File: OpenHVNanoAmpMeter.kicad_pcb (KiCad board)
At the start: 4 copper layers, 64.5 x 38 mm, 70 parts, among them J1 Conn_Coaxial, J2 Conn_Coaxial, J3 AVR-ISP-6, J4 Barrel_Jack_Switch, U1 DDC112U, U10 NCP1117-5.0_SOT223, U11 NCP1117-5.0_SOT223, U2 ATmega328PB-M, U3 74LV8154, U4 74LS151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

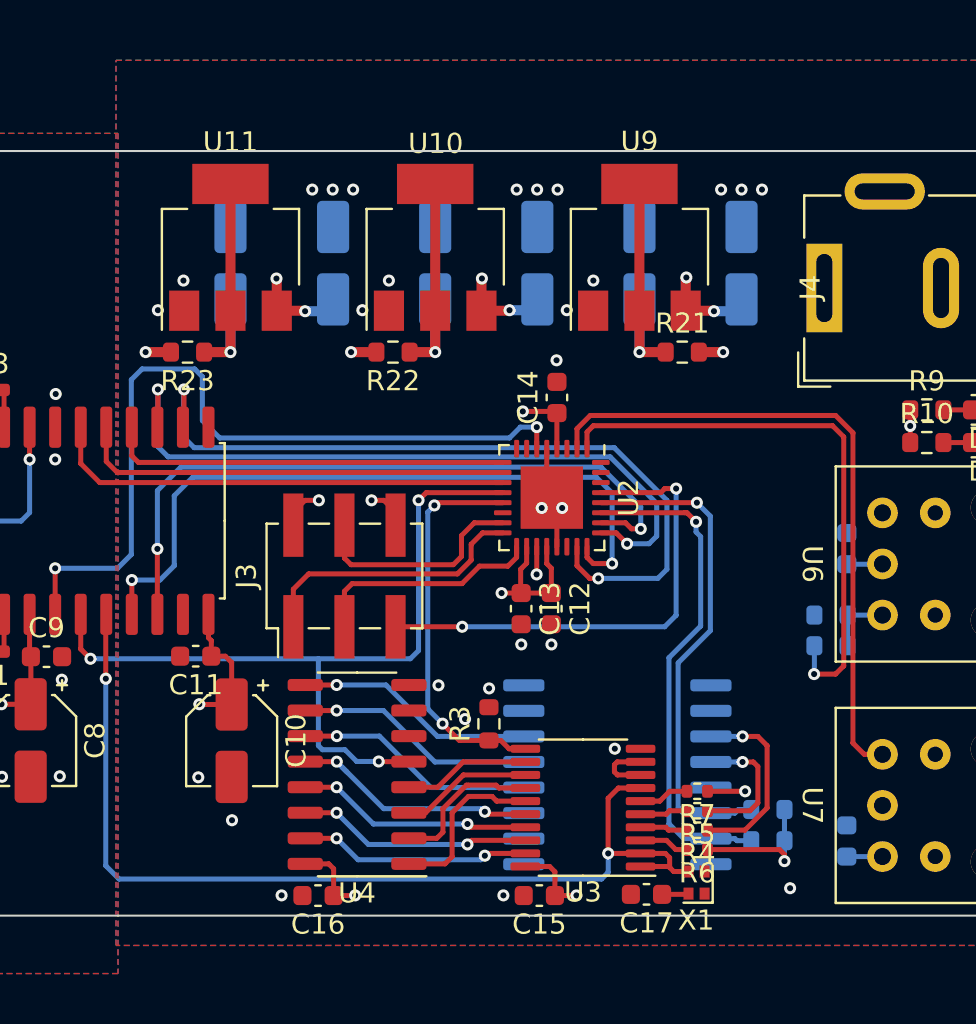
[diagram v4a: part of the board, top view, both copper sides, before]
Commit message: updated 10MHz oscillator to DIP 14 package
needs larger PCB space, but much easier to purchase
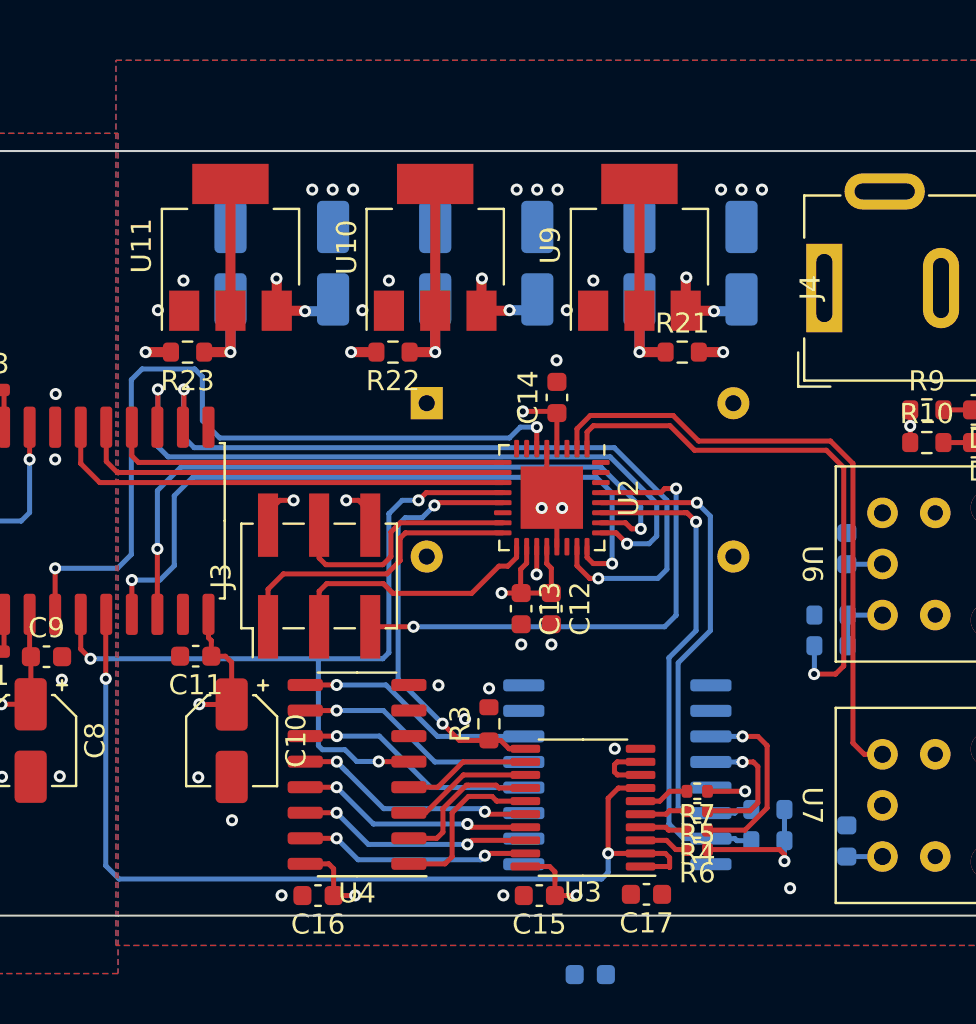
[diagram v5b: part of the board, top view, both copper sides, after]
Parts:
- added C28: 100n, Capacitor_SMD:C_0603_1608Metric, B.Cu at (96.4, 74.9)
- X1: value ASCO -> CXO_DIP14; footprint Oscillator:Oscillator_SMD_Abracon_ASCO-4Pin_1.6x1.2mm -> Oscillator:Oscillator_DIP-14; moved to B.Cu
- moved X1 27.3 mm to (88.3, 46.5), turned to 0 degrees
- moved J3 1.26 mm to (82.9, 55.1)
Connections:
- X1 pad 1: unconnected-(X1-Pad1) -> +5VD
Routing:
- net +3V3: track 16.7 -> 4.74 mm
- net /Clock Generation/CNT_CLR: track 19.4 -> 21.1 mm
- net /DataProcessing/SCK: track 11.5 -> 13.2 mm
- net /DataProcessing/MISO: track 13.9 -> 15.3 mm
- net /DataProcessing/MOSI: track 11.1 -> 12.5 mm
- net +5VD: track 38.8 -> 37.5 mm
- net /DataProcessing/~{RESET}: track 24.3 -> 25.6 mm
- net /Clock Generation/CLK_10MHz: track 49.5 -> 48.4 mm
- net /DataProcessing/LWLRX: track 32.5 -> 31.6 mm
- net /DataProcessing/LWLTX: track 28.4 -> 27.5 mm

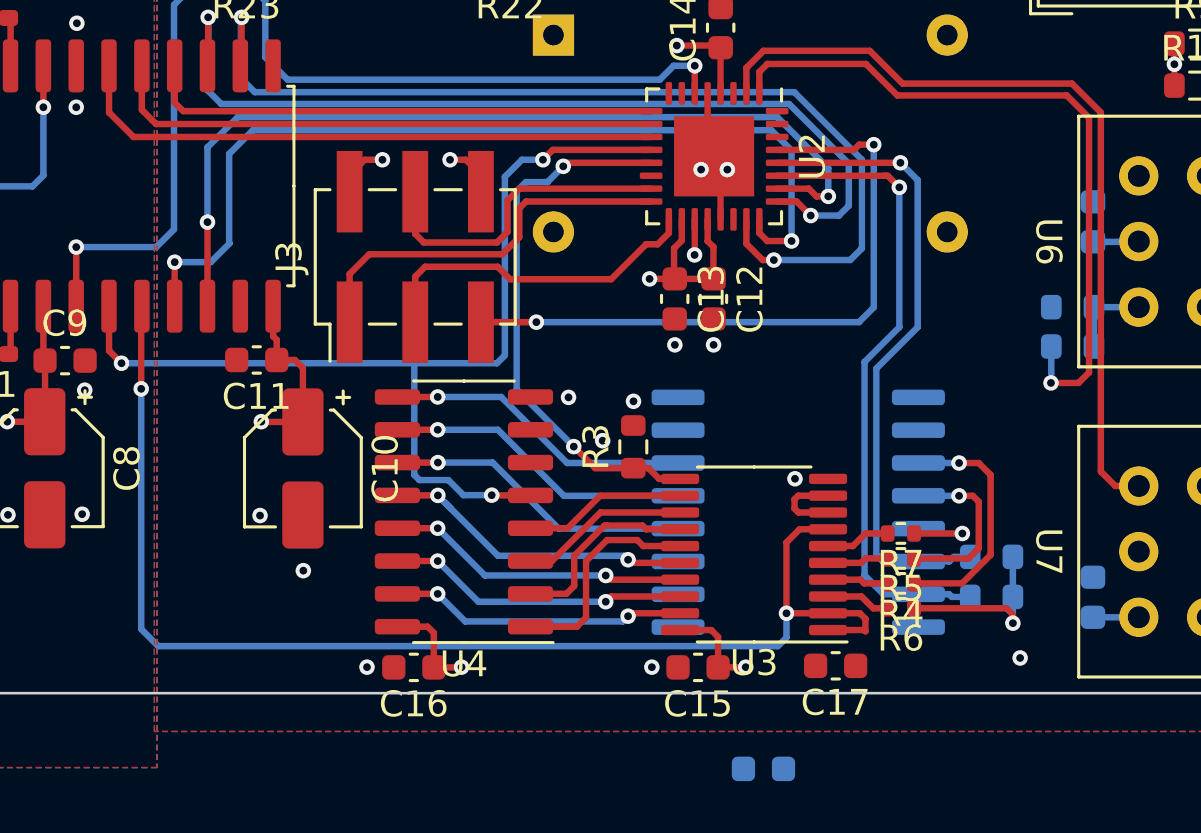
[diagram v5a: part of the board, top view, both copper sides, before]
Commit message: inlcuded buffer for 10MHz clock
otherwise the oscillator does not have enough drive strength
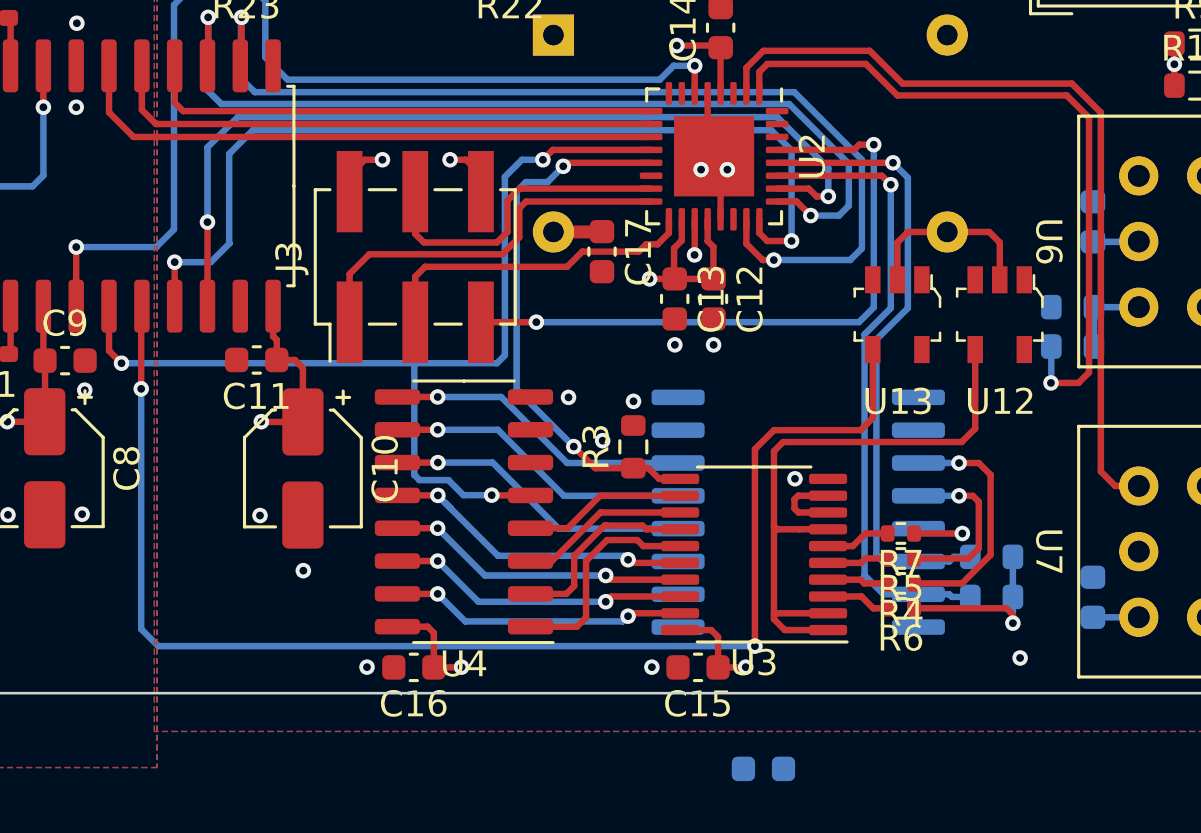
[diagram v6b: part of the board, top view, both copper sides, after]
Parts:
- added U12: SN74LVC1G17DBVR, digikey-footprints:SOT-753, F.Cu at (105.6, 57.4)
- added U13: SN74LVC1G17DBVR, digikey-footprints:SOT-753, F.Cu at (101.6, 57.4)
- moved C17 18.4 mm to (90.2, 54.9), turned to -90 degrees
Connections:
- U3 pad 1: /Clock Generation/CLK_10MHz -> Net-(U3-Pad1)
- U3 pad 2: /Clock Generation/CLK_10MHz -> Net-(U3-Pad1)
- U3 pad 7: /Clock Generation/CLK_10MHz -> Net-(U3-Pad1)
- X1 pad 8: /Clock Generation/CLK_10MHz -> Net-(X1-Pad8)
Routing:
- net Net-(U3-Pad1): track 0.00 -> 24.2 mm
- net Net-(X1-Pad8): track 0.00 -> 7.19 mm
- net /Clock Generation/CLK_10MHz: track 48.4 -> 51.8 mm
- net +5VD: track 37.5 -> 39.4 mm

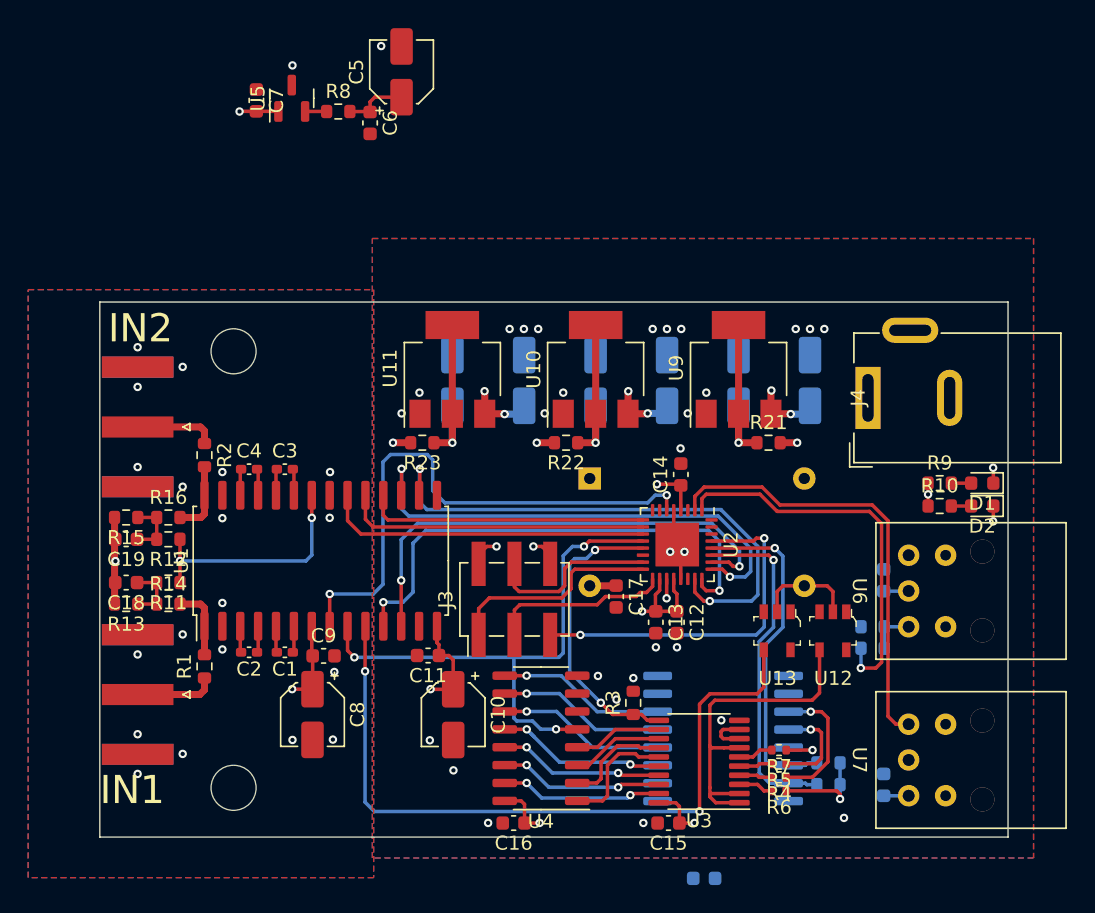
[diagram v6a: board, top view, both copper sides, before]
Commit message: added buffer to ref voltage generation
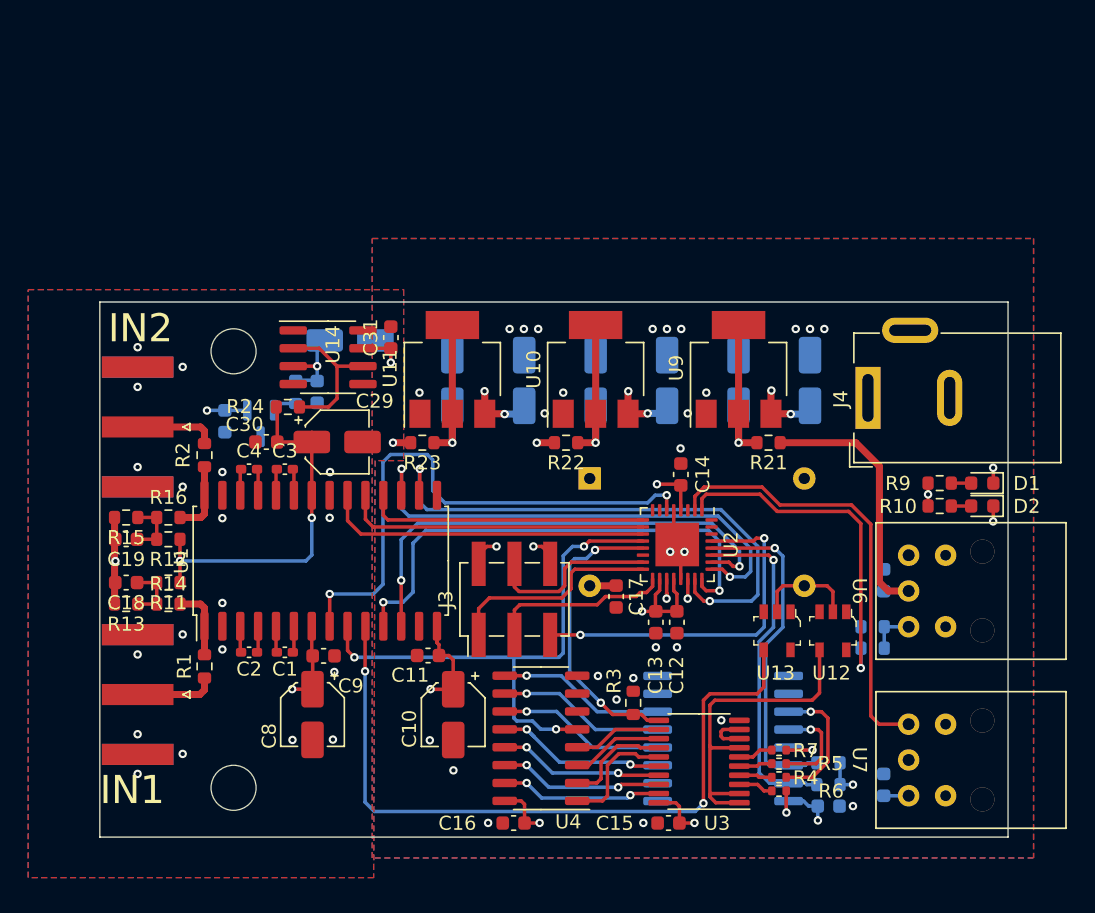
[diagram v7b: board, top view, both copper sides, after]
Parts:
- added C29: 10u, Capacitor_SMD:CP_Elec_4x3.9, F.Cu at (70.4, 43.9)
- added C30: 100n, Capacitor_SMD:C_0603_1608Metric, F.Cu at (65.3, 43.9)
- added C31: 100n, Capacitor_SMD:C_0603_1608Metric, F.Cu at (74.2, 36.5)
- added R24: R, Resistor_SMD:R_0603_1608Metric, F.Cu at (66.9, 41.5)
- added U14: OPA340UA, Package_SO:SOIC-8_3.9x4.9mm_P1.27mm, F.Cu at (69.7, 37.9)
- C5, C6, C7, R8, U5: moved to B.Cu
- moved U5 23.2 mm to (64.9, 42.6), turned to -90 degrees
- moved C7 22.9 mm to (62.4, 42.5), turned to 90 degrees
- moved R8 20.1 mm to (67.4, 40.4), turned to 90 degrees
- moved C6 19.5 mm to (68.9, 40.4)
- moved C5 19.4 mm to (71.3, 36.7), turned to 0 degrees
- moved C28 10.2 mm to (105.3, 69.8), turned to 0 degrees
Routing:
- net Net-(D1-Pad1): track 1.10 -> 32.7 mm, vias 1 -> 2
- net Net-(D2-Pad1): track 2.48 -> 32.2 mm
- net +3V3: track 4.74 -> 21.8 mm, vias 1 -> 0
- net Net-(R24-Pad1): track 0.00 -> 10.7 mm
- net /CurrentMeasurement/VREF: track 16.9 -> 26.2 mm
- net +5VA: track 10.6 -> 13.7 mm, vias 3 -> 4
- net /DataProcessing/LWLTX: track 27.5 -> 24.8 mm
- net Net-(C5-Pad1): track 4.49 -> 5.72 mm, vias 0 -> 1
- net +5VD: track 39.4 -> 39.8 mm, vias 10 -> 12
- net GNDA: vias 22 -> 20
- net GND: vias 30 -> 29

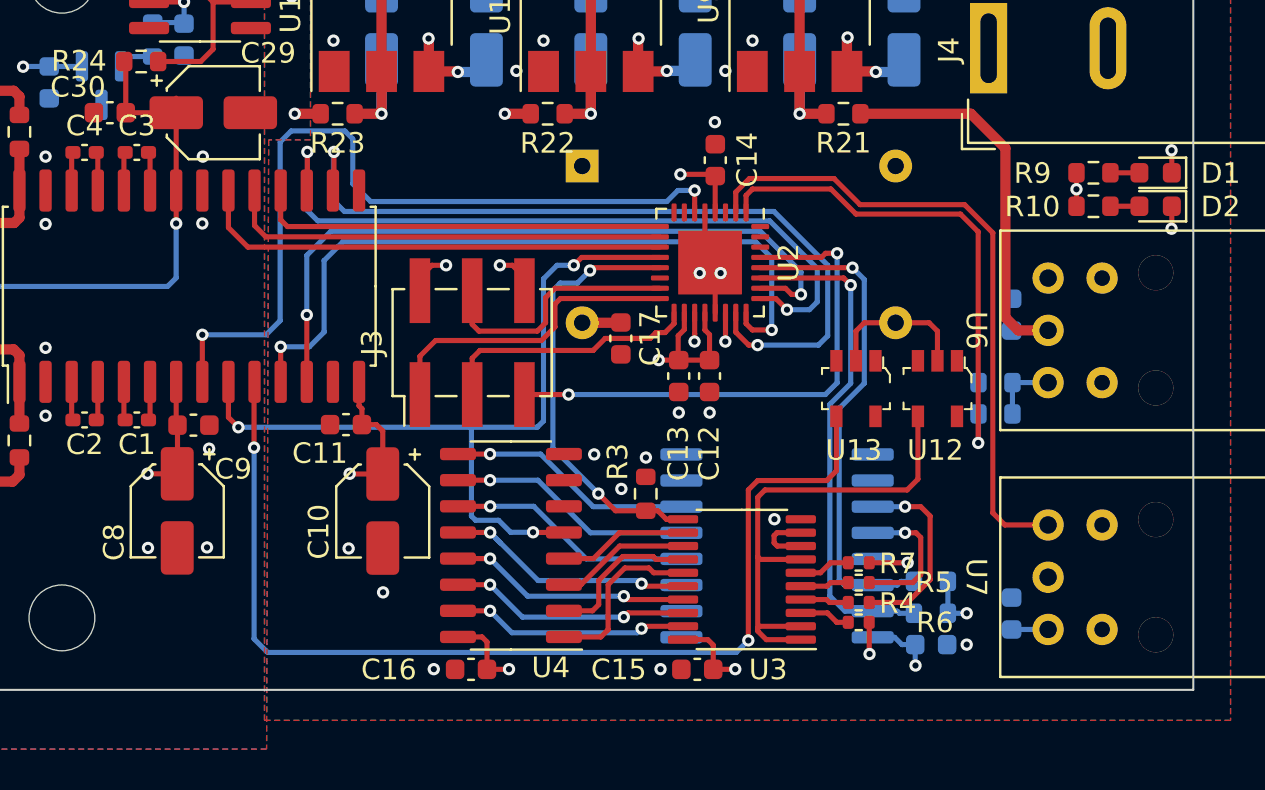
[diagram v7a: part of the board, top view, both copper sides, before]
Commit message: added MadeByJochen + GPL symbol
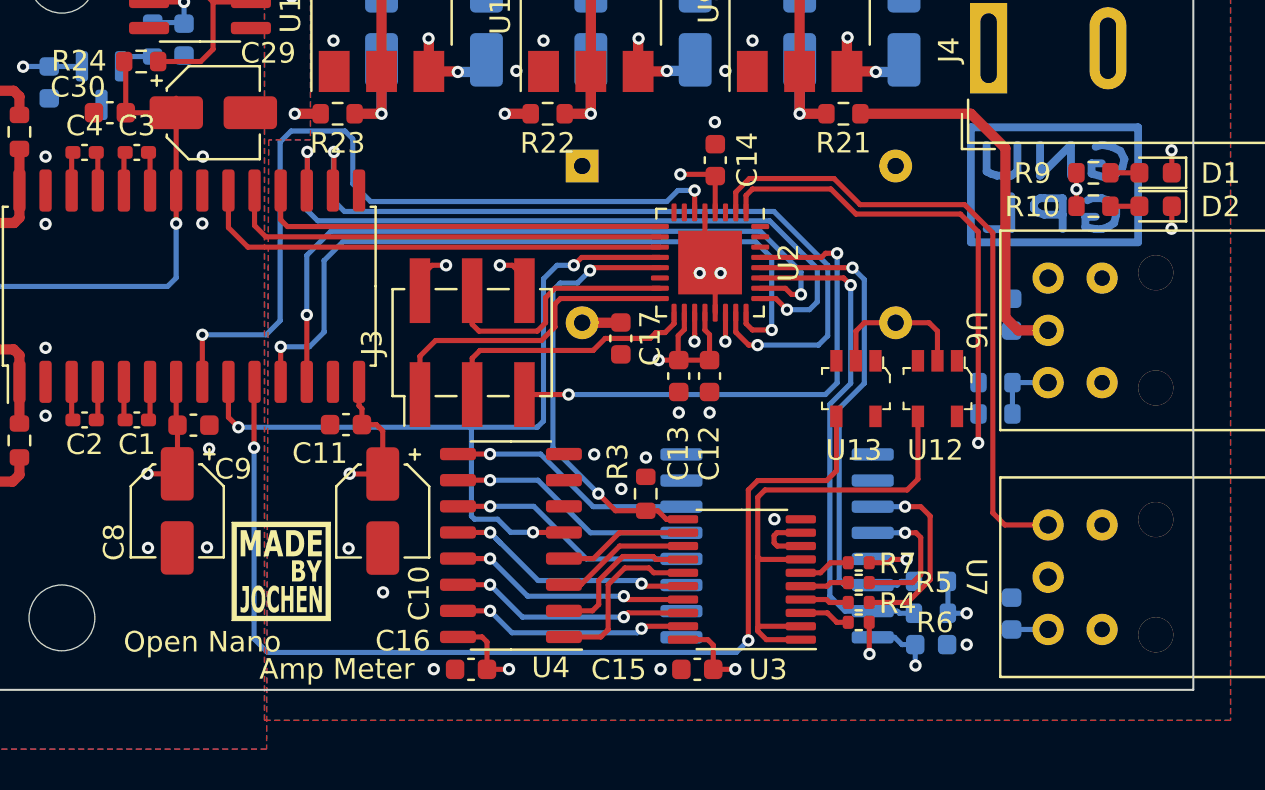
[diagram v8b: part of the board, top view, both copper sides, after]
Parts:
- added G***: LOGO, MadeByJochen:MadeByJochen_5x5, F.Cu at (73.7, 66.3)
- added REF**: Symbol_GNU-GPL_CopperTop_Small, Symbol:Symbol_GNU-GPL_CopperTop_Small, B.Cu at (111.3, 47.7)
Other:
- board text added: "Amp Meter"
- board text added: "Open Nano"
